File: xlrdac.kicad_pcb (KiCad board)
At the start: 2 copper layers, 144.8 x 137.1 mm, 27 parts, among them J1 StereoIn, J2 Left Output, J3 Right Output, J4 PWR ENTRY, U1 THAT1646, U2 THAT1646

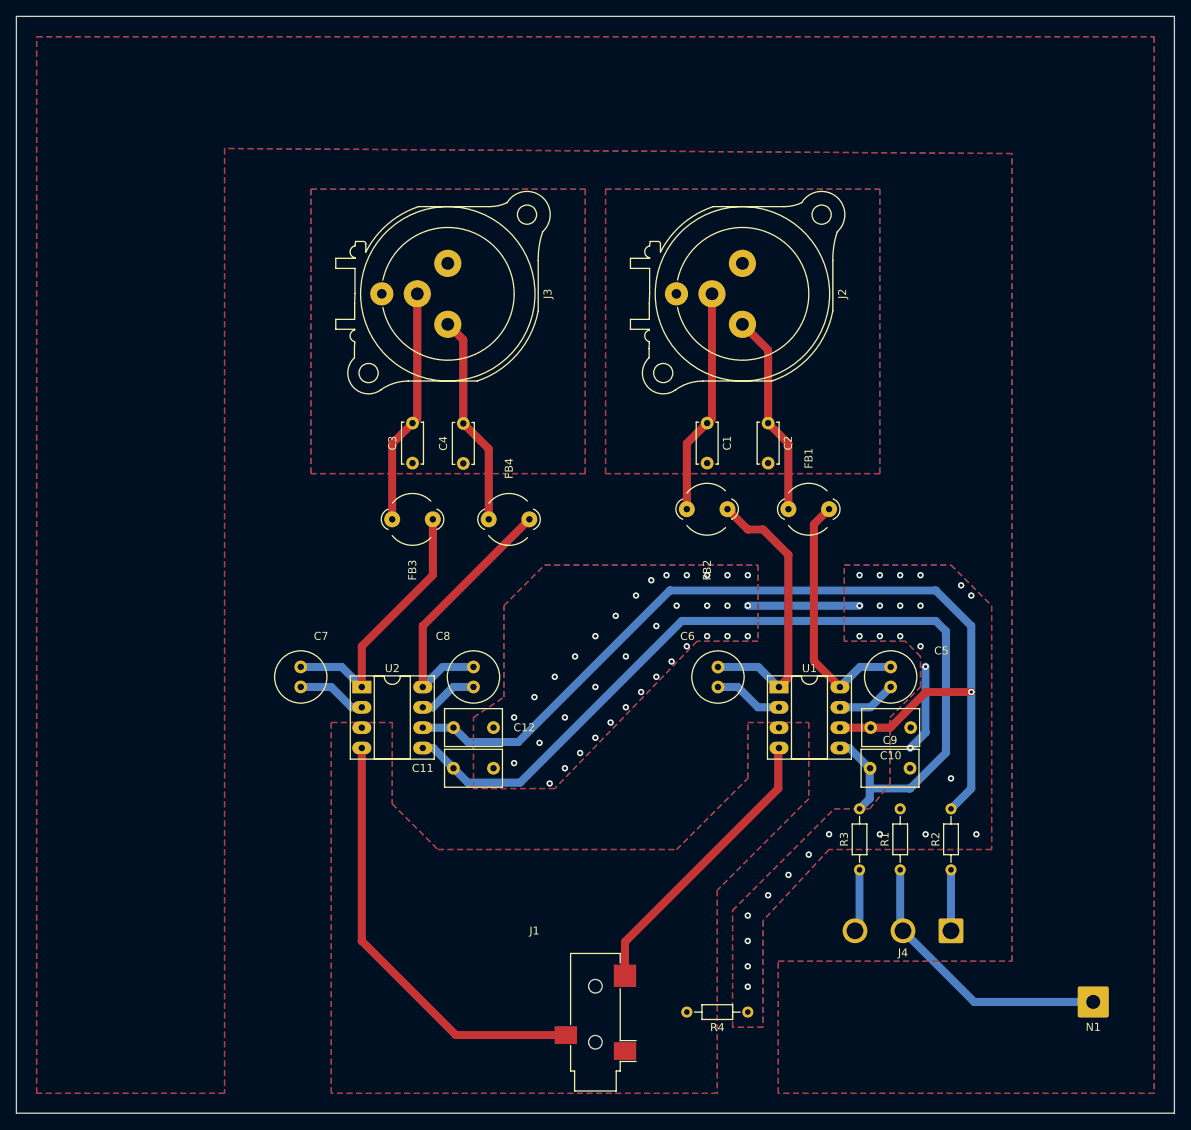
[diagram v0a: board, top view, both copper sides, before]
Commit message: Move line drivers to dedicated file
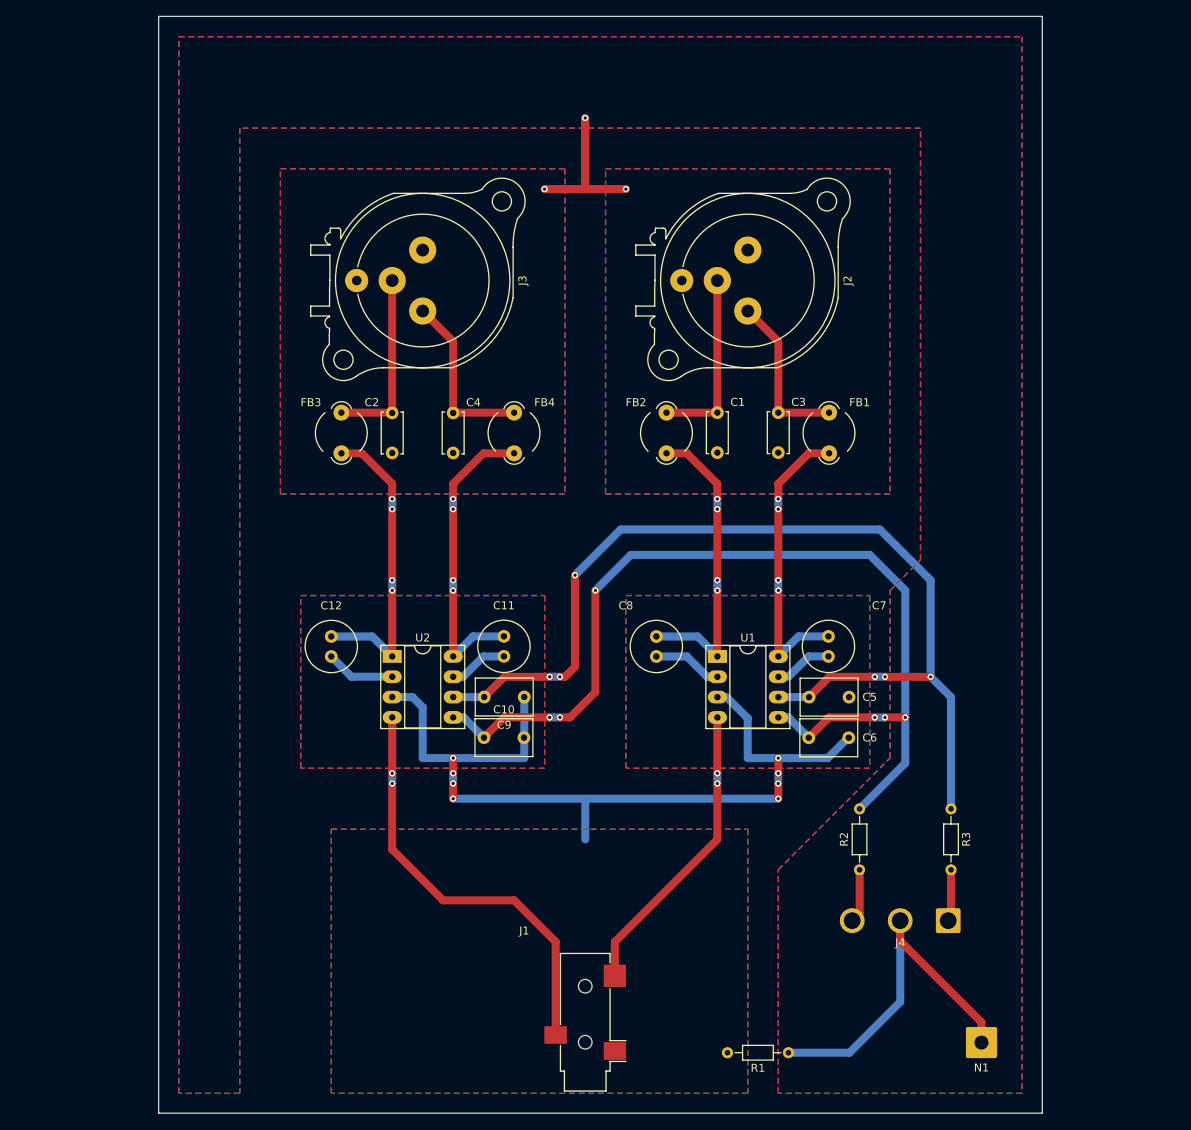
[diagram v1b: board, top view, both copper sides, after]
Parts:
- removed R4: 0R, Resistor_THT:R_Axial_DIN0204_L3.6mm_D1.6mm_P7.62mm_Horizontal
- C11, C12: value 100nF -> 10uF NP; footprint Capacitor_THT:C_Rect_L7.0mm_W4.5mm_P5.00mm -> Capacitor_THT:C_Radial_D6.3mm_H11.0mm_P2.50mm
- C5, C6: value 10uF NP -> 100nF; footprint Capacitor_THT:C_Radial_D6.3mm_H11.0mm_P2.50mm -> Capacitor_THT:C_Rect_L7.0mm_W4.5mm_P5.00mm
- moved C7 66.1 mm to (126.9, 116.8)
- moved C10 53.4 mm to (83.9, 127.0), turned to 0 degrees
- moved C2 47.1 mm to (72.4, 91.4), turned to 90 degrees
- moved C3 46.2 mm to (120.7, 86.4), turned to -90 degrees
- moved C9 44.1 mm to (88.9, 121.9), turned to 180 degrees
- moved R1 26.8 mm to (121.9, 166.4), turned to 180 degrees
- moved C8 23.2 mm to (105.4, 116.8)
- moved C12 22.1 mm to (64.8, 116.8), turned to 90 degrees
- moved C11 15.3 mm to (86.4, 116.8), turned to 90 degrees
- moved N1 14.9 mm to (146.1, 165.1)
- moved FB3 14.1 mm to (66.0, 91.4), turned to 90 degrees
- moved R3 13.7 mm to (142.2, 135.9), turned to -90 degrees
- moved C6 13.0 mm to (124.5, 127.0), turned to 0 degrees
- moved R2 11.4 mm to (130.8, 143.5)
- moved FB2 10.3 mm to (106.7, 91.4), turned to 90 degrees
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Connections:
- net Net-(J1-PadR) renamed /Line Driver Right/IN
- net Net-(J1-PadT) renamed /Line Driver Left/IN
- C1 pad 2: Net-(C1-Pad2) -> PWR.GND
- C10 pad 1: GNDPWR -> VEE
- C10 pad 2: VCC -> GNDA
- C11 pad 1: VEE -> Net-(C11-Pad1)
- C11 pad 2: GNDPWR -> /Line Driver Right/OUT+
- C12 pad 1: GNDPWR -> Net-(C12-Pad1)
- C12 pad 2: VCC -> /Line Driver Right/OUT-
- C2 pad 1: Net-(C2-Pad1) -> PWR.GND
- C2 pad 2: Net-(C1-Pad2) -> Net-(C2-Pad2)
- C3 pad 2: Net-(C3-Pad2) -> PWR.GND
- C4 pad 1: Net-(C3-Pad1) -> PWR.GND
- C5 pad 1: Net-(C5-Pad1) -> GNDA
- C5 pad 2: Net-(C5-Pad2) -> VCC
- C6 pad 1: Net-(C6-Pad1) -> VEE
- C6 pad 2: Net-(C6-Pad2) -> GNDA
- C7 pad 2: Net-(C7-Pad2) -> /Line Driver Left/OUT+
- C8 pad 2: Net-(C8-Pad2) -> /Line Driver Left/OUT-
- C9 pad 1: VEE -> GNDA
- C9 pad 2: GNDPWR -> VCC
- FB1 pad 1: Net-(C5-Pad2) -> /Line Driver Left/OUT+
- FB1 pad 2: Net-(C2-Pad1) -> Net-(C3-Pad1)
- FB2 pad 1: Net-(C6-Pad2) -> /Line Driver Left/OUT-
- FB3 pad 1: Net-(C7-Pad2) -> /Line Driver Right/OUT-
- FB3 pad 2: Net-(C3-Pad2) -> Net-(C2-Pad2)
- FB4 pad 1: Net-(C8-Pad2) -> /Line Driver Right/OUT+
- J2 pad 1: Net-(C1-Pad2) -> PWR.GND
- J2 pad 2: Net-(C2-Pad1) -> Net-(C3-Pad1)
- J2 pad G: Net-(C1-Pad2) -> PWR.GND
- J3 pad 1: Net-(C3-Pad1) -> PWR.GND
- J3 pad 3: Net-(C3-Pad2) -> Net-(C2-Pad2)
- J3 pad G: Net-(C3-Pad1) -> PWR.GND
- R1 pad 2: GNDPWR -> GNDA
- R2 pad 1: PWR.VCC -> PWR.VEE
- R2 pad 2: VCC -> VEE
- R3 pad 1: PWR.VEE -> VCC
- R3 pad 2: VEE -> PWR.VCC
- U1 pad 1: Net-(C6-Pad2) -> /Line Driver Left/OUT-
- U1 pad 2: Net-(C6-Pad1) -> Net-(C8-Pad1)
- U1 pad 7: Net-(C5-Pad1) -> Net-(C7-Pad1)
- U1 pad 8: Net-(C5-Pad2) -> /Line Driver Left/OUT+
- U2 pad 1: Net-(C7-Pad2) -> /Line Driver Right/OUT-
- U2 pad 2: Net-(C7-Pad1) -> Net-(C12-Pad1)
- U2 pad 7: Net-(C8-Pad1) -> Net-(C11-Pad1)
- U2 pad 8: Net-(C8-Pad2) -> /Line Driver Right/OUT+
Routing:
- net GNDA: track 0.72 -> 109.2 mm, vias 0 -> 8
- net PWR.GND: track 35.2 -> 84.3 mm, vias 0 -> 3
- net /Line Driver Left/OUT-: track 0.00 -> 38.2 mm, vias 0 -> 4
- net /Line Driver Right/OUT+: track 0.00 -> 38.2 mm, vias 0 -> 4
- net /Line Driver Right/OUT-: track 0.00 -> 38.2 mm, vias 0 -> 4
- net /Line Driver Left/OUT+: track 0.00 -> 36.9 mm, vias 0 -> 4
- net Net-(C6-Pad2): track 35.7 -> 0.00 mm
- net Net-(C8-Pad2): track 33.9 -> 0.00 mm
- net Net-(C7-Pad2): track 33.3 -> 0.00 mm
- net Net-(C5-Pad2): track 31.8 -> 0.00 mm
- net Net-(C3-Pad2): track 29.5 -> 0.00 mm
- net Net-(C2-Pad1): track 25.5 -> 0.00 mm
- net GNDPWR: track 24.9 -> 0.00 mm, vias 64 -> 0
- net Net-(C2-Pad2): track 0.00 -> 22.9 mm
- net Net-(C3-Pad1): track 0.00 -> 20.6 mm
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- removed copper zone on B.Cu, net GNDPWR
- removed copper zone on F.Cu, net GNDPWR
- removed copper zone on B.Cu, net Net-(C1-Pad2)
- removed copper zone on F.Cu, net Net-(C1-Pad2)
- removed copper zone on B.Cu, net Net-(C3-Pad1)
- removed copper zone on F.Cu, net Net-(C3-Pad1)
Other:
- board size 144.8 x 137.1 mm -> 110.5 x 137.1 mm
